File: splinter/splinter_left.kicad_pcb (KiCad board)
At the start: 2 copper layers, 117.5 x 89.9 mm, 19 parts, among them SW10 SW_Push, SW11 SW_Push, SW12 SW_Push, SW14 SW_Push, SW15 SW_Push, SW16 SW_Push, SW17 SW_Push, SW18 SW_Push, SW20 SW_Push, SW21 SW_Push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

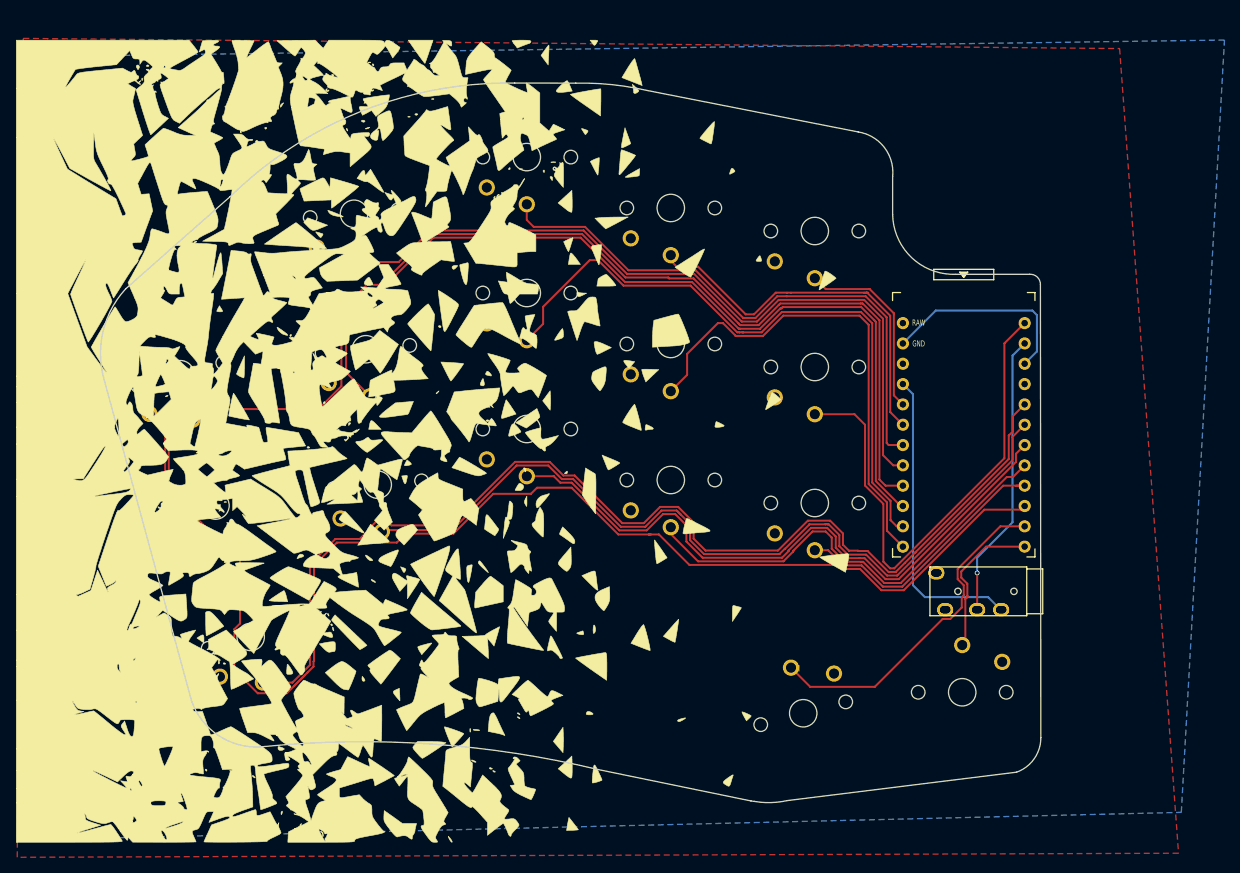
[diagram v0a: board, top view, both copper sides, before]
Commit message: Add splinter pcb
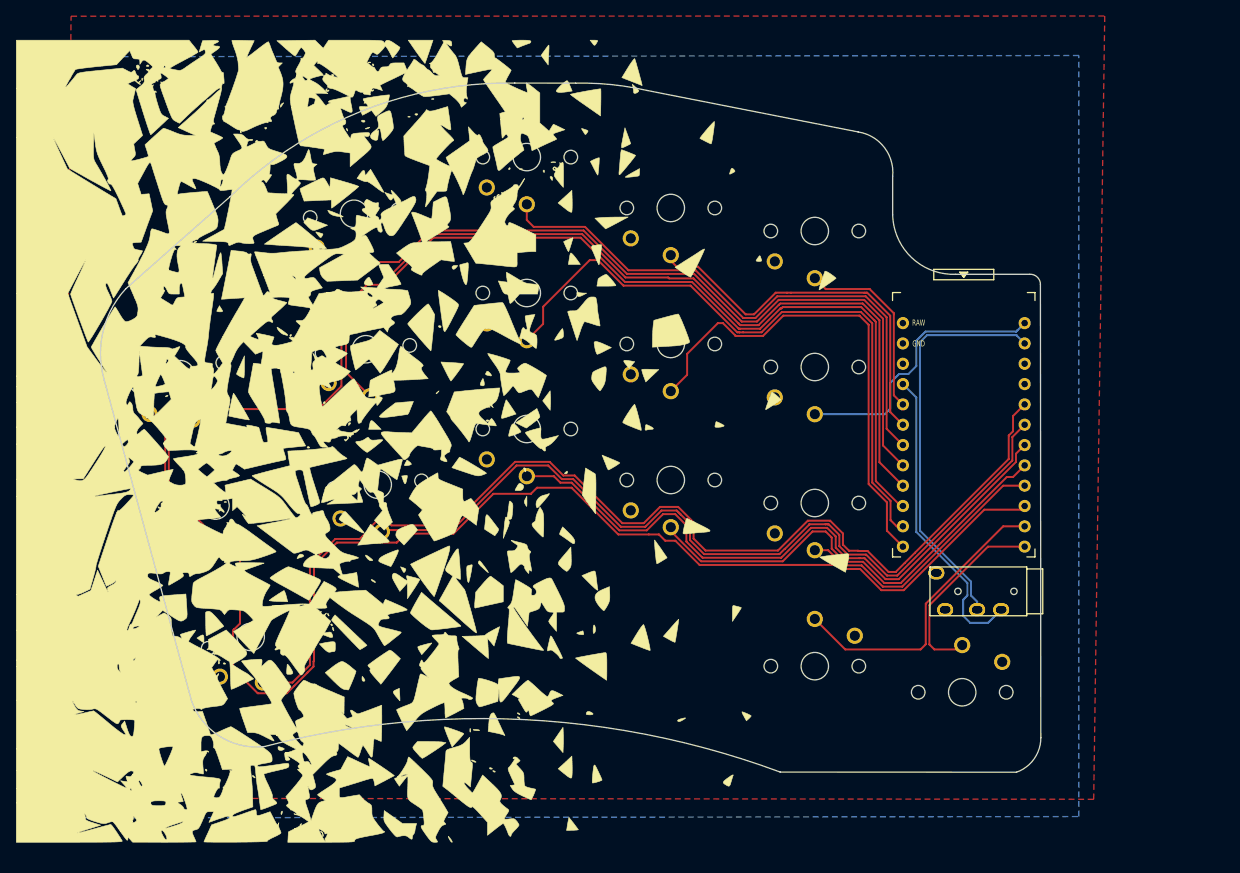
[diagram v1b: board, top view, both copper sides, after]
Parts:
- moved SW20 6.06 mm to (183.8, 114.0), turned to 180 degrees
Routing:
- net Switch10: track 64.0 -> 34.7 mm
- net gnd: track 25.9 -> 0.50 mm
- net Switch18: track 35.8 -> 50.3 mm, vias 1 -> 0
- net Switch16: track 43.9 -> 37.2 mm
- net Switch17: track 19.9 -> 24.4 mm
- net Switch1: track 168.5 -> 166.6 mm
- net Switch6: track 153.6 -> 152.4 mm
- net Switch2: track 94.9 -> 93.7 mm
- net Switch15: track 34.4 -> 33.3 mm
- net Switch3: track 72.1 -> 71.0 mm
- net Switch14: track 58.0 -> 57.4 mm
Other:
- board size 117.5 x 89.9 mm -> 117.5 x 86.1 mm
